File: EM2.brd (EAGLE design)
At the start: 101.6 x 53.3 mm, 114 parts, among them IC1 EUP3476SO08T, IC2 APX811-44UG-7, IC3 ATMEGA16U2-MU, IC4 MCP24AA025E48, IC6 W5500, IC9 ATMEGA2560-16AU, J1 DC_2_1MM, P1 USB-6PSMT, P3 ICSP:USB, P4 microSD, Q2 2N7002, U1 HY931147C-RJ45, X1 16MHz, X2 25MHz, X3 16MHz

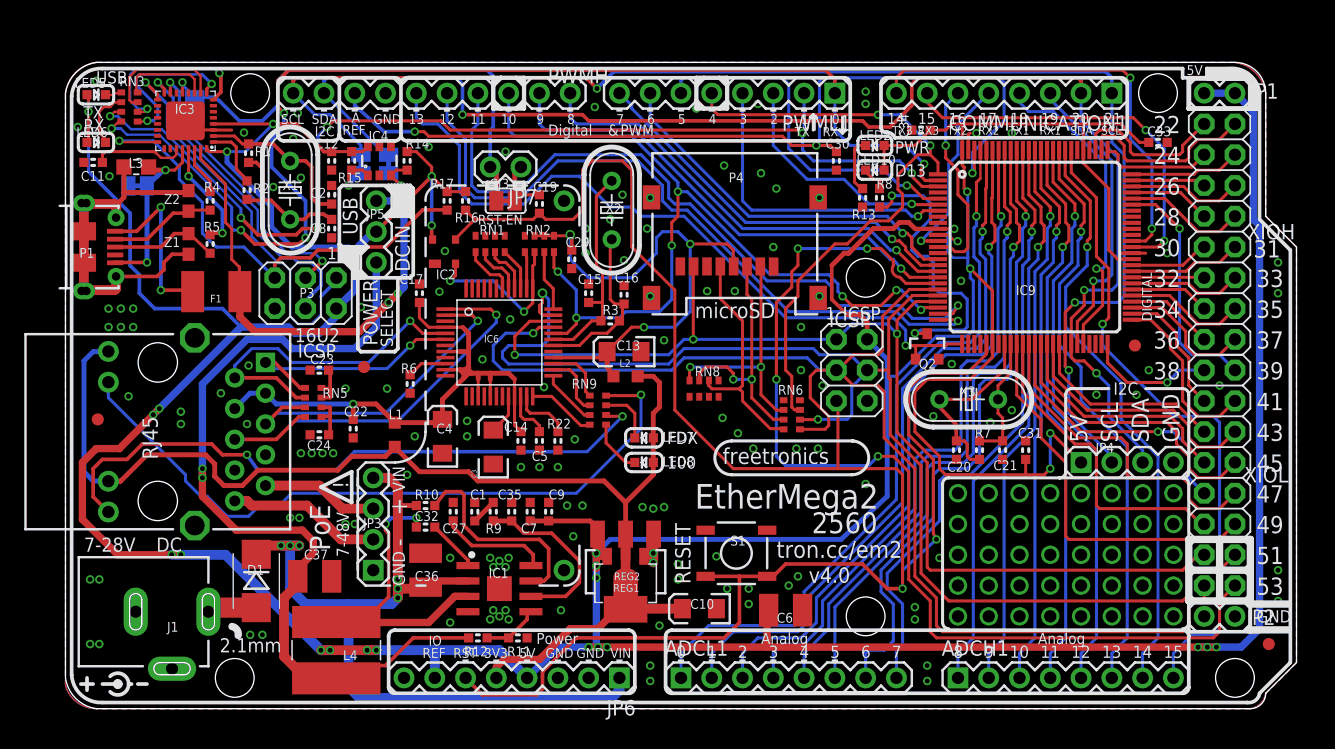
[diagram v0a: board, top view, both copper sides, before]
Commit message: Changed USB socket
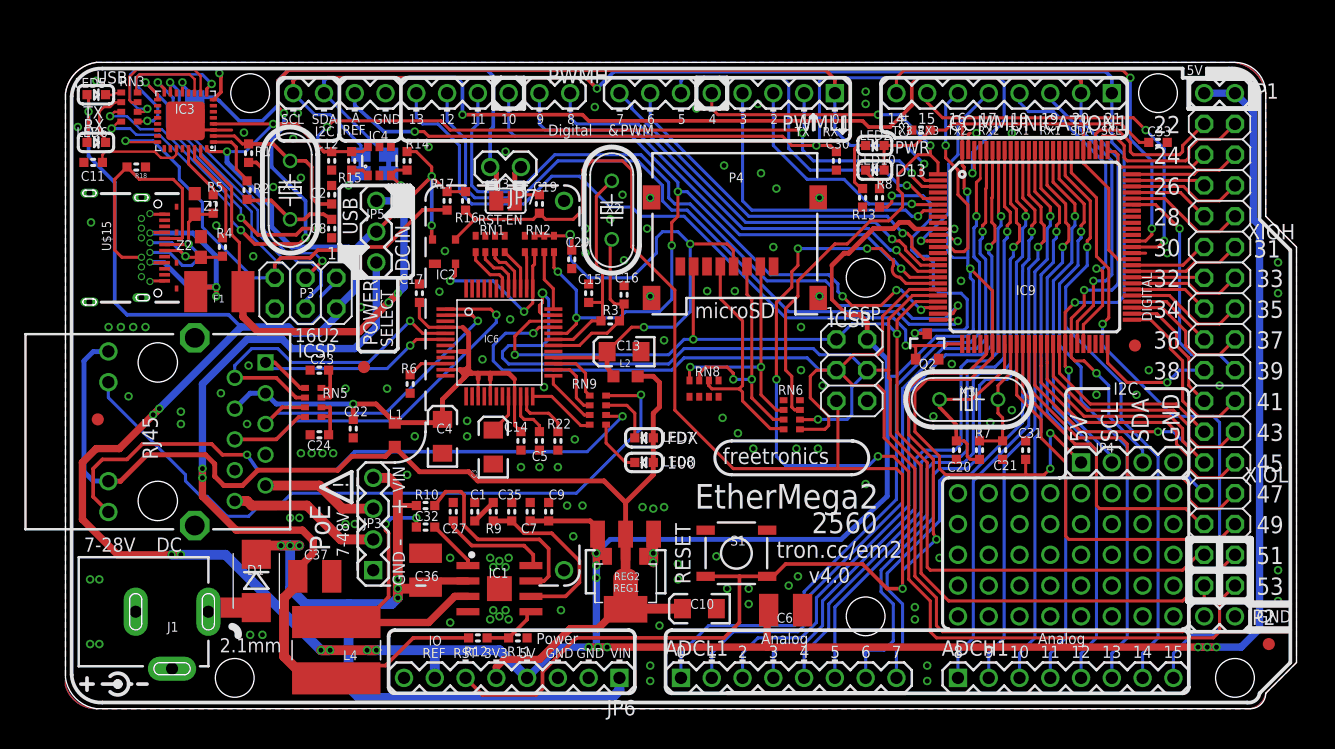
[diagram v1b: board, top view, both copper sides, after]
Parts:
- removed L3: 0805 INDUCTOR, freetronics-master-v1:0805-LARGE
- removed P1: USB-6PSMT, freetronics-jon:USB-MICROB-MB05PMXX
- removed SJ1: GROUND, freetronics-jon:SJC
- added R18: 5.1K, freetronics-original:0603
- added U$15: USB-C, freetronics-jon:USB-C-U52A
- moved R4 3.94 mm to (13.0, 38.1)
- moved Z2 3.94 mm to (11.2, 38.1)
- moved Z1 3.34 mm to (10.7, 41.7), turned to 90 degrees
- moved R5 3.31 mm to (12.2, 41.7)
- moved F1 0.25 mm to (12.7, 34.4)
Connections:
- removed net N$115: F1.1, P1.VBUS
- removed net N$16: P1.D+, R5.2, Z1.1
- removed net N$17: P1.D-, R4.2, Z2.1
- removed net N$18: L3.1, P1.FIX1, P1.FIX2, P1.PIN1, P1.PIN2, P1.TAB1, P1.TAB2, Z1.2, Z2.2
- removed net N$74: IC3.28, L3.2, P1.GND, SJ1.1
- new net D+: R5.2, U$15.A6, U$15.B6, Z1.1
- new net D-: R4.2, U$15.A7, U$15.B7, Z2.1
- new net N$67: R18.2, U$15.A5, U$15.B5
- new net USB+: F1.1, U$15.A4, U$15.A9, U$15.B4, U$15.B9
- net GND: now also IC3.28, R18.1, U$15.A1, U$15.A12, U$15.B1, U$15.B12, U$15.CASE1, U$15.CASE2, U$15.CASE3, U$15.CASE4, U$15.FIX1, U$15.FIX2, U$15.FIX3, U$15.FIX4, Z1.2, Z2.2; no longer SJ1.2
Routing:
- net N$18: track 30.5 -> 0.00 mm
- net N$67: track 0.00 -> 20.6 mm
- net USB+: track 0.00 -> 20.2 mm, vias 0 -> 2
- net N$74: track 15.7 -> 0.00 mm, vias 2 -> 0
- net N$115: track 14.1 -> 0.00 mm, vias 2 -> 0
- net D+: track 0.00 -> 12.4 mm, vias 0 -> 1
- net N$16: track 9.06 -> 0.00 mm
- net N$17: track 8.89 -> 0.00 mm
- net D-: track 0.00 -> 8.44 mm, vias 0 -> 1
- net RD+: track 9.24 -> 4.64 mm, vias 2 -> 0
- net RD-: track 4.10 -> 8.54 mm
- net GND: track 13.7 -> 15.4 mm
- net 5V: track 474.6 -> 476.0 mm
- net RESET2: track 40.0 -> 38.7 mm
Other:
- board text added: "EM2"
- board text removed: "EM"
- board text removed: "EtherMega"

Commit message: Library part migration to SuperHouse
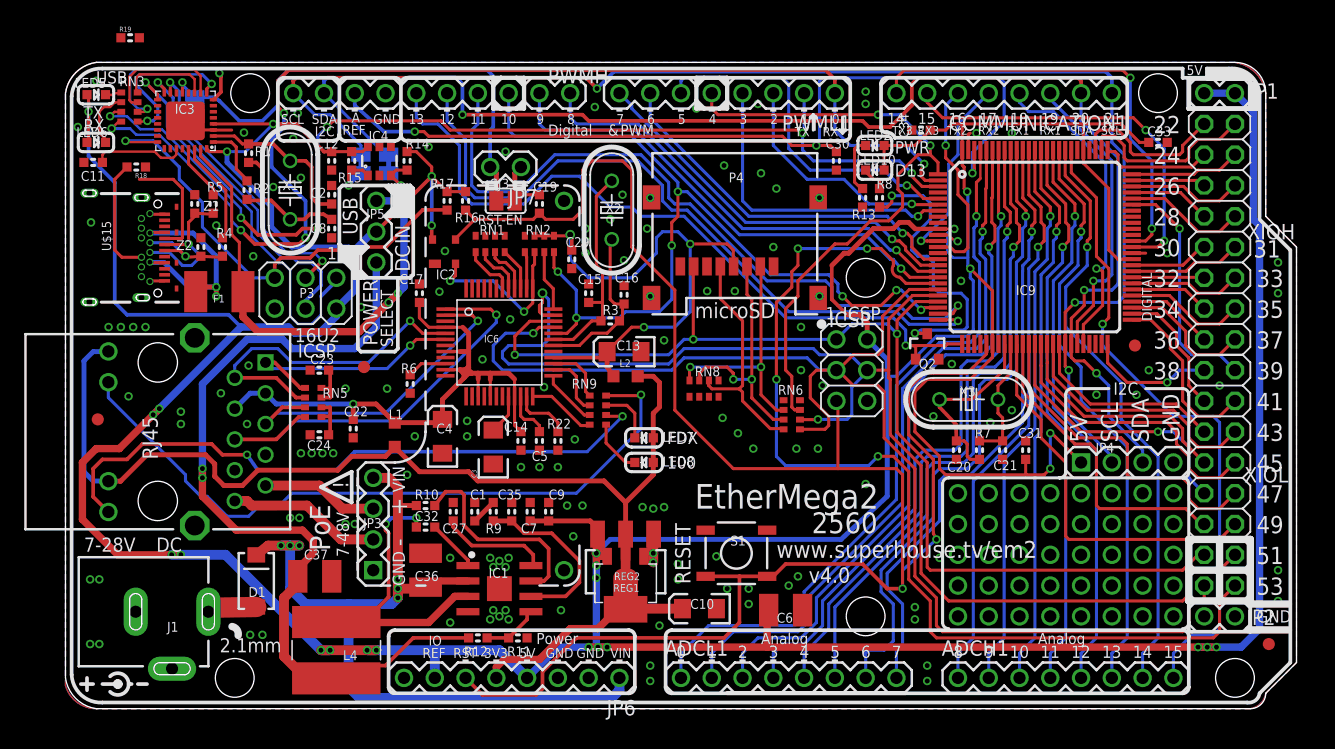
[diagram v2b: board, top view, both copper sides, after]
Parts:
- added R19: 5.1K, SuperHouse-DiscreteSemi:R0603
- ADCH1, ADCL1, COMMUNICATION1, JP6, PWML1: value (none) -> M08-SOCKET; device freetronics-master-v1.1:1X08 -> SuperHouse-Connectors:1X08-S
- C1, C12, C15, C16, C19, C2, C20, C21, C22, C23, C24, C27, C29, C30, C31, C32, C33, C34, C35, C7, C8, C9: device freetronics-marc:0603 -> SuperHouse-DiscreteSemi:C0603
- C11: device freetronics-master-v1:0603 -> SuperHouse-DiscreteSemi:C0603
- C14, C17, C5: device freetronics-jon:0603 -> SuperHouse-DiscreteSemi:C0603
- D1: value 1N4004 SMB -> 1N4004 SMA; device freetronics:SMB-DIODE -> SuperHouse-DiscreteSemi:SMA-DIODE
- F1: device rcl:L1812 -> SuperHouse-Fuses:1812
- IC6: device W5500:W5500 -> SuperHouse-ICs:W5500
- IC9: device atmel-2005:TQFP100 -> SuperHouse-MCUs:TQFP100
- ICSP, P3: device pinhead:2X03 -> SuperHouse-Connectors:2X03-ICSP
- J1: device freetronics-jon:POWER_JACK_PTH_SLOTS -> SuperHouse-Connectors:POWER_JACK_SLOTS
- JP5: device freetronics-master-v1.1:1X03 -> SuperHouse-Connectors:1X03-P
- LED10, LED2, LED5, LED6, LED7, LED8: device freetronics-jon:LED-0603 -> SuperHouse-LEDs:LED-0603
- PWMH: value (none) -> M10-SOCKET; device freetronics-original:1X10 -> SuperHouse-Connectors:1X10-S
- Q2: device freetronics:SOT23-3 -> SuperHouse-DiscreteSemi:SOT23-3
- R1, R13, R16, R17, R2, R22, R3, R4, R5, R6, R7, R8: device freetronics-marc:0603 -> SuperHouse-DiscreteSemi:R0603
- R10, R11, R12, R18, R9: device freetronics-original:0603 -> SuperHouse-DiscreteSemi:R0603
- R14, R15: device freetronics-master-v1.1:0603 -> SuperHouse-DiscreteSemi:R0603
- RN1, RN2, RN9: device freetronics-master-v1.1:CAY16 -> SuperHouse-DiscreteSemi:CAY16
- RN3, RN5, RN6, RN8: device freetronics-master-v1:CAY16 -> SuperHouse-DiscreteSemi:CAY16
- S1: device freetronics:TACTILE_SWITCH_SMD -> SuperHouse-Switches:TACTILE_SMT-6MM
- U$15: device freetronics-jon:USB-C-U52A -> SuperHouse-Connectors:USB-C-U52A
- U1: device freetronics-jon:HY931147C -> SuperHouse-Connectors:HY931147C
- X1, X2, X3: device freetronics-master-v1:HC49U-V -> SuperHouse-Oscillators:HC49U-V
- Z1, Z2: device freetronics:0603 -> SuperHouse-DiscreteSemi:TVS0603
- turned D1 to 90 degrees
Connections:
- new net N$14: R18.2, U$15.B5
- net GND: now also R19.1
- net N$67: now also R19.2; no longer R18.2, U$15.B5
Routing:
- net N$67: track 20.6 -> 9.43 mm
- net N$14: track 0.00 -> 9.73 mm
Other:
- board text added: "by Jonathan Oxer"
- board text added: "www.superhouse.tv/em2"
- board text removed: "by Jonathan Oxer and Marc Alexander"
- board text removed: "freetronics"
- board text removed: "tron.cc/em2"
- board text removed: "www.freetronics.com.au/em2"
